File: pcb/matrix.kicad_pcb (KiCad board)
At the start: 2 copper layers, 57.4 x 47.1 mm, 69 parts, among them J1 Conn_01x02, J2 USB_C_Receptacle_USB2.0_14P, SW1 SW_Push, SW2 SW_Push, SW3 SW_Push, SW4 SW_Push, U1 ESP32-S3-MINI-1U, U2 AP2112K-3.3

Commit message: Update silkscreen
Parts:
- renumbered TP9 to 3V3, TP8 to BAT, TP1 to CP1, TP2 to CP2, TP3 to CP3, TP4 to CP4, TP5 to CP5, TP6 to CP6, TP7 to GND, TP10 to USB
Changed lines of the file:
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@@
 			(at 0 -1.43 90)
 			(layer "F.SilkS")
+			(hide yes)
 			(effects
 				(font
@@
 			(at 0 -1.43 0)
 			(layer "F.SilkS")
+			(hide yes)
 			(effects
 				(font
@@
 			(at 0 -1.43 0)
 			(layer "F.SilkS")
+			(hide yes)
 			(effects
 				(font
@@
 		(descr "SMD pad as test Point, diameter 1.0mm")
 		(tags "test point SMD pad")
-		(property "Reference" "TP7"
+		(property "Reference" "GND"
 			(at 0 -1.448 0)
 			(layer "F.SilkS")
@@
 			(at 0 -1.43 90)
 			(layer "F.SilkS")
+			(hide yes)
 			(effects
 				(font
@@
 			(at 0 -1.43 0)
 			(layer "F.SilkS")
+			(hide yes)
 			(effects
 				(font
@@
 			(at 0 -1.43 90)
 			(layer "F.SilkS")
+			(hide yes)
 			(effects
 				(font
@@
 			(at 0 -1.43 90)
 			(layer "F.SilkS")
+			(hide yes)
 			(effects
 				(font
@@
 			(at 0 -1.68 90)
 			(layer "F.SilkS")
+			(hide yes)
 			(effects
 				(font
@@
 			(at 0 -1.43 90)
 			(layer "F.SilkS")
+			(hide yes)
 			(effects
 				(font
@@
 			(at 0.0375 -1.68 90)
 			(layer "F.SilkS")
+			(hide yes)
 			(effects
 				(font
@@
 			(at 0 -1.68 90)
 			(layer "F.SilkS")
+			(hide yes)
 			(effects
 				(font
@@
 			(at 0 -1.68 90)
 			(layer "F.SilkS")
+			(hide yes)
 			(effects
 				(font
@@
 		(descr "SMD pad as test Point, diameter 1.0mm")
 		(tags "test point SMD pad")
-		(property "Reference" "TP4"
+		(property "Reference" "CP4"
 			(at 0 -1.448 0)
 			(layer "F.SilkS")
@@
 			(at 0 -1.43 0)
 			(layer "F.SilkS")
+			(hide yes)
 			(effects
 				(font
@@
 		(descr "SMD pad as test Point, diameter 1.0mm")
 		(tags "test point SMD pad")
-		(property "Reference" "TP6"
+		(property "Reference" "CP6"
 			(at 0 -1.448 0)
 			(layer "F.SilkS")
@@
 			(at 0 -1.43 90)
 			(layer "F.SilkS")
+			(hide yes)
 			(effects
 				(font
@@
 			(at 0 -1.43 90)
 			(layer "F.SilkS")
+			(hide yes)
 			(effects
 				(font
@@
 			(at 0 -1.68 90)
 			(layer "F.SilkS")
+			(hide yes)
 			(effects
 				(font
@@
 			(at 0 -1.43 0)
 			(layer "F.SilkS")
+			(hide yes)
 			(effects
 				(font
@@
 			(at 0 -1.43 90)
 			(layer "F.SilkS")
+			(hide yes)
 			(effects
 				(font
@@
 			(at 0 -1.43 90)
 			(layer "F.SilkS")
+			(hide yes)
 			(effects
 				(font
@@
 			(at 0 -1.43 0)
 			(layer "F.SilkS")
+			(hide yes)
 			(effects
 				(font
@@
 			(at 0 -1.43 0)
 			(layer "F.SilkS")
+			(hide yes)
 			(effects
 				(font
@@
 			(at 0 -1.43 90)
 			(layer "F.SilkS")
+			(hide yes)
 			(effects
 				(font
@@
 			(at 0 -1.68 90)
 			(layer "F.SilkS")
+			(hide yes)
 			(effects
 				(font
@@
 			(at 0 -1.43 0)
 			(layer "F.SilkS")
+			(hide yes)
 			(effects
 				(font
@@
 			(at 0 -1.68 90)
 			(layer "F.SilkS")
+			(hide yes)
 			(effects
 				(font
@@
 			(at 0 -1.43 0)
 			(layer "F.SilkS")
+			(hide yes)
 			(effects
 				(font
@@
 			(at 0 -1.43 0)
 			(layer "F.SilkS")
+			(hide yes)
 			(effects
 				(font
@@
 			(at 0 -1.68 90)
 			(layer "F.SilkS")
+			(hide yes)
 			(effects
 				(font
@@
 		(descr "SMD pad as test Point, diameter 1.0mm")
 		(tags "test point SMD pad")
-		(property "Reference" "TP9"
+		(property "Reference" "3V3"
 			(at 0 -1.448 0)
 			(layer "F.SilkS")
@@
 			(at 0 -1.43 0)
 			(layer "F.SilkS")
+			(hide yes)
 			(effects
 				(font
@@
 		(descr "SMD pad as test Point, diameter 1.0mm")
 		(tags "test point SMD pad")
-		(property "Reference" "TP2"
+		(property "Reference" "CP2"
 			(at 0 -1.448 0)
 			(layer "F.SilkS")
@@
 			(at 0 -1.68 90)
 			(layer "F.SilkS")
+			(hide yes)
 			(effects
 				(font
@@
 			(at 0 -1.43 90)
 			(layer "F.SilkS")
+			(hide yes)
 			(effects
 				(font
@@
 			(at 0 -1.43 90)
 			(layer "F.SilkS")
+			(hide yes)
 			(effects
 				(font
@@
 		(descr "SMD pad as test Point, diameter 1.0mm")
 		(tags "test point SMD pad")
-		(property "Reference" "TP10"
+		(property "Reference" "USB"
 			(at 0 -1.448 0)
 			(layer "F.SilkS")
@@
 			(at 0 -1.68 90)
 			(layer "F.SilkS")
+			(hide yes)
 			(effects
 				(font
@@
 			(at 0 -1.68 90)
 			(layer "F.SilkS")
+			(hide yes)
 			(effects
 				(font
@@
 			(at 0 -1.68 90)
 			(layer "F.SilkS")
+			(hide yes)
 			(effects
 				(font
@@
 			(at 0 -1.43 0)
 			(layer "F.SilkS")
+			(hide yes)
 			(effects
 				(font
@@
 			(at 0 -1.68 90)
 			(layer "F.SilkS")
+			(hide yes)
 			(effects
 				(font
@@
 			(at 0 -1.68 90)
 			(layer "F.SilkS")
+			(hide yes)
 			(effects
 				(font
@@
 		(descr "SMD pad as test Point, diameter 1.0mm")
 		(tags "test point SMD pad")
-		(property "Reference" "TP5"
+		(property "Reference" "CP5"
 			(at 0 -1.448 0)
 			(layer "F.SilkS")
@@
 			(at 0 -1.43 0)
 			(layer "F.SilkS")
+			(hide yes)
 			(effects
 				(font
@@
 			(at 0 -1.43 0)
 			(layer "F.SilkS")
+			(hide yes)
 			(effects
 				(font
@@
 		(descr "SMD pad as test Point, diameter 1.0mm")
 		(tags "test point SMD pad")
-		(property "Reference" "TP8"
+		(property "Reference" "BAT"
 			(at 0 -1.448 0)
 			(layer "F.SilkS")
@@
 		(descr "SMD pad as test Point, diameter 1.0mm")
 		(tags "test point SMD pad")
-		(property "Reference" "TP3"
+		(property "Reference" "CP3"
 			(at 0 -1.447869 0)
 			(layer "F.SilkS")
@@
 			(at 0 -1.68 90)
 			(layer "F.SilkS")
+			(hide yes)
 			(effects
 				(font
@@
 			(at 0.0375 -1.68 90)
 			(layer "F.SilkS")
+			(hide yes)
 			(effects
 				(font
@@
 			(at 0 -1.43 0)
 			(layer "F.SilkS")
+			(hide yes)
 			(effects
 				(font
@@
 			(at 0 -1.68 90)
 			(layer "F.SilkS")
+			(hide yes)
 			(effects
 				(font
@@
 			(at 0.0375 -1.68 90)
 			(layer "F.SilkS")
+			(hide yes)
 			(effects
 				(font
@@
 			(at 0.0375 -1.68 90)
 			(layer "F.SilkS")
+			(hide yes)
 			(effects
 				(font
@@
 		(descr "SMD pad as test Point, diameter 1.0mm")
 		(tags "test point SMD pad")
-		(property "Reference" "TP1"
+		(property "Reference" "CP1"
 			(at 0 -1.448 0)
 			(layer "F.SilkS")
@@
 			(at 0 -1.43 0)
 			(layer "F.SilkS")
+			(hide yes)
 			(effects
 				(font
@@
 			(at 0 -1.43 0)
 			(layer "F.SilkS")
+			(hide yes)
 			(effects
 				(font
@@
 			(at 0 -1.43 0)
 			(layer "F.SilkS")
+			(hide yes)
 			(effects
 				(font
@@
 			(at 0.0375 -1.68 90)
 			(layer "F.SilkS")
+			(hide yes)
 			(effects
 				(font
@@
 			(at 0 -1.43 0)
 			(layer "F.SilkS")
+			(hide yes)
 			(effects
 				(font

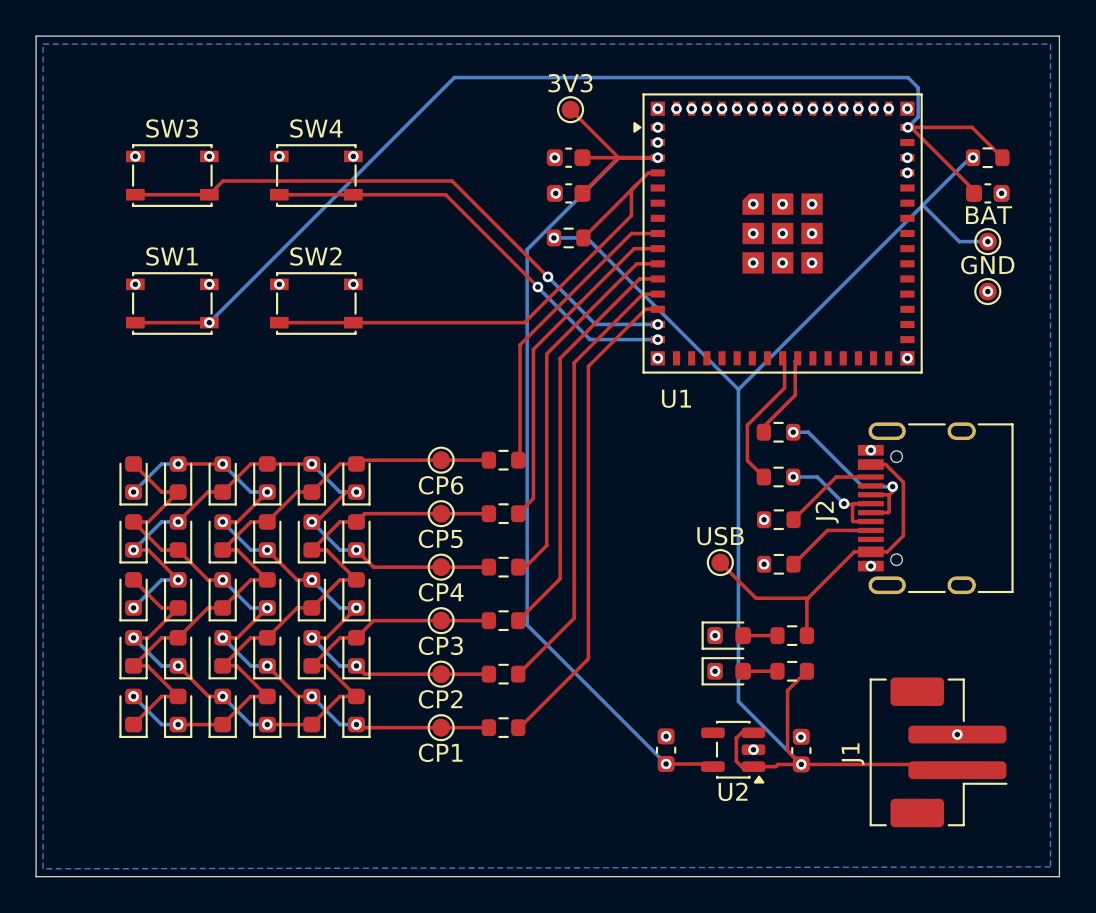
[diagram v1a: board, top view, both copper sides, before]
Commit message: Fix incorrect voltage
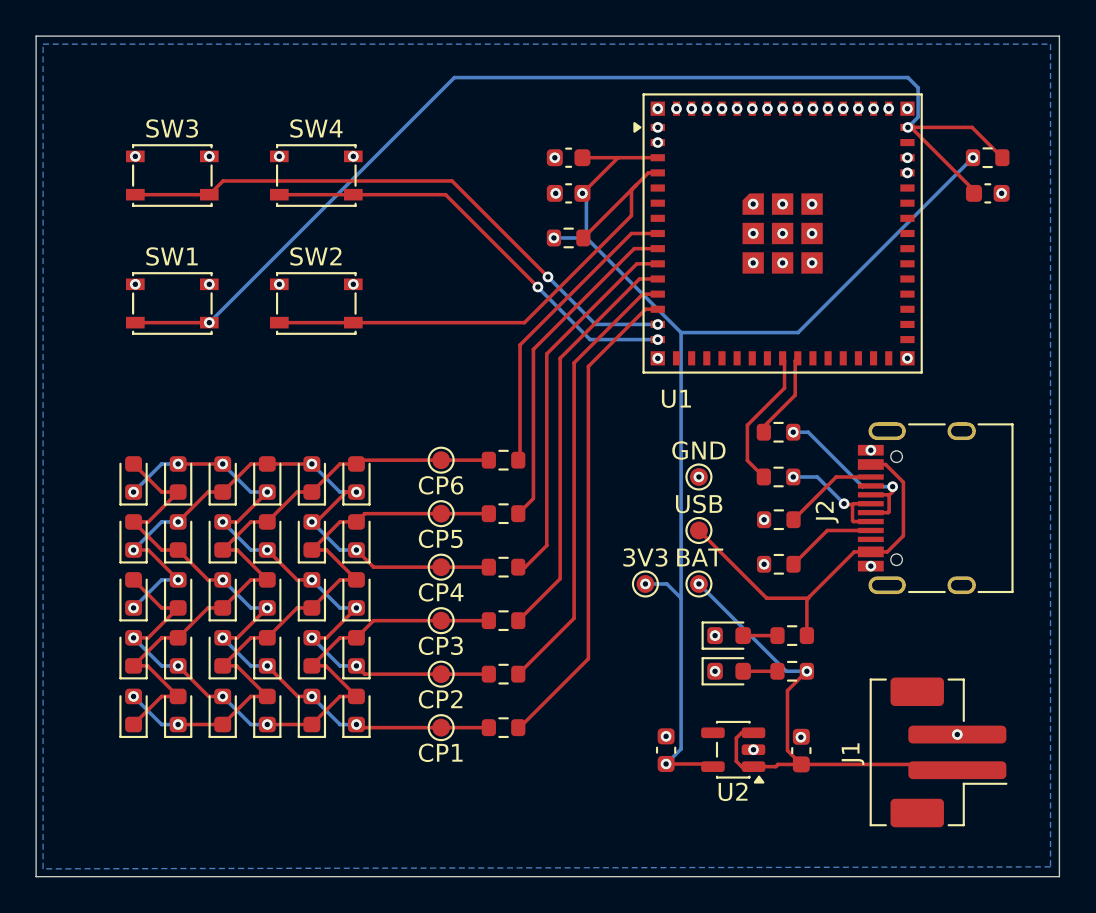
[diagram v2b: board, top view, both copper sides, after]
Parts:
- moved 3V3 26.9 mm to (149.2, 108.0)
- moved BAT 25.1 mm to (152.2, 108.0)
- moved GND 19.3 mm to (152.2, 102.0)
- moved USB 2.16 mm to (152.2, 105.0)
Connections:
- R3 pad 2: Net-(J1-Pin_1) -> Net-(U1-3V3)
- R4 pad 2: Net-(J1-Pin_1) -> Net-(U1-3V3)
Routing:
- net Net-(J1-Pin_1): track 80.9 -> 29.5 mm, vias 4 -> 2
- net Net-(U1-3V3): track 57.3 -> 69.1 mm, vias 2 -> 5
- net Net-(J2-VBUS-PadA4): track 20.0 -> 21.9 mm
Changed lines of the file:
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@@
 			(layers "F.Cu" "F.Mask" "F.Paste")
 			(roundrect_rratio 0.25)
-			(net 1 "Net-(J1-Pin_1)")
+			(net 3 "Net-(U1-3V3)")
 			(pintype "passive")
 		)
@@
 	(footprint "TestPoint:TestPoint_Pad_D1.0mm"
 		(layer "F.Cu")
-		(at 168.4 91.6)
+		(at 152.2 102)
 		(descr "SMD pad as test Point, diameter 1.0mm")
 		(tags "test point SMD pad")
@@
 			(layers "F.Cu" "F.Mask" "F.Paste")
 			(roundrect_rratio 0.25)
-			(net 1 "Net-(J1-Pin_1)")
+			(net 3 "Net-(U1-3V3)")
 			(pintype "passive")
 		)
@@
 	(footprint "TestPoint:TestPoint_Pad_D1.0mm"
 		(layer "F.Cu")
-		(at 145 81.4)
+		(at 149.2 108)
 		(descr "SMD pad as test Point, diameter 1.0mm")
 		(tags "test point SMD pad")
@@
 	(footprint "TestPoint:TestPoint_Pad_D1.0mm"
 		(layer "F.Cu")
-		(at 153.4 106.8)
+		(at 152.2 105)
 		(descr "SMD pad as test Point, diameter 1.0mm")
 		(tags "test point SMD pad")
@@
 	(footprint "TestPoint:TestPoint_Pad_D1.0mm"
 		(layer "F.Cu")
-		(at 168.4 88.8)
+		(at 152.2 108)
 		(descr "SMD pad as test Point, diameter 1.0mm")
 		(tags "test point SMD pad")
@@
 	)
 	(segment
-		(start 167.5675 84.095)
-		(end 167.4175 84.095)
-		(width 0.2)
-		(layer "F.Cu")
-		(net 1)
-	)
-	(segment
 		(start 156.51 118.245)
 		(end 156.635 118.12)
@@
 	)
 	(via
-		(at 167.5675 84.095)
-		(size 0.6)
-		(drill 0.3)
-		(layers "F.Cu" "B.Cu")
-		(net 1)
-	)
-	(via
-		(at 168.4 88.8)
-		(size 0.6)
-		(drill 0.3)
-		(layers "F.Cu" "B.Cu")
-		(net 1)
-	)
-	(via
-		(at 157.9425 118.12)
+		(at 158.254265 112.895735)
 		(size 0.6)
 		(drill 0.3)
@@
 	)
 	(via
-		(at 144.0675 88.595)
+		(at 152.2 108)
 		(size 0.6)
 		(drill 0.3)
@@
 	)
 	(segment
-		(start 167.5675 84.095)
-		(end 167.4175 84.095)
-		(width 0.2)
-		(layer "B.Cu")
-		(net 1)
-	)
-	(segment
-		(start 167.4175 84.095)
-		(end 165.05625 86.45625)
-		(width 0.2)
-		(layer "B.Cu")
-		(net 1)
-	)
-	(segment
-		(start 154.4175 97.095)
-		(end 145.9175 88.595)
-		(width 0.2)
-		(layer "B.Cu")
-		(net 1)
-	)
-	(segment
-		(start 168.4 88.8)
-		(end 166.8 88.8)
-		(width 0.2)
-		(layer "B.Cu")
-		(net 1)
-	)
-	(segment
-		(start 154.4175 114.595)
-		(end 154.4175 97.095)
-		(width 0.2)
-		(layer "B.Cu")
-		(net 1)
-	)
-	(segment
-		(start 145.9175 88.595)
-		(end 144.0675 88.595)
-		(width 0.2)
-		(layer "B.Cu")
-		(net 1)
-	)
-	(segment
-		(start 166.8 88.8)
-		(end 164.75625 86.75625)
-		(width 0.2)
-		(layer "B.Cu")
-		(net 1)
-	)
-	(segment
-		(start 165.05625 86.45625)
-		(end 164.75625 86.75625)
-		(width 0.2)
-		(layer "B.Cu")
-		(net 1)
-	)
-	(segment
-		(start 157.9425 118.12)
-		(end 154.4175 114.595)
+		(start 158.254265 112.895735)
+		(end 157.095735 112.895735)
 		(width 0.2)
 		(layer "B.Cu")
@@
 	)
 	(segment
-		(start 164.75625 86.75625)
-		(end 154.4175 97.095)
+		(start 157.095735 112.895735)
+		(end 152.2 108)
 		(width 0.2)
 		(layer "B.Cu")
@@
 	)
 	(via
-		(at 168.4 91.6)
+		(at 152.2 102)
 		(size 0.6)
 		(drill 0.3)
@@
 	)
 	(segment
+		(start 145.6675 84.095)
+		(end 149.8925 84.095)
+		(width 0.2)
+		(layer "F.Cu")
+		(net 3)
+	)
+	(segment
 		(start 152.835735 118.095735)
 		(end 152.985 118.245)
@@
 	)
 	(segment
-		(start 145.6675 84.095)
-		(end 149.8925 84.095)
-		(width 0.2)
-		(layer "F.Cu")
-		(net 3)
-	)
-	(segment
-		(start 145 81.4)
-		(end 147.695 84.095)
+		(start 167.5675 84.095)
+		(end 167.4175 84.095)
 		(width 0.2)
 		(layer "F.Cu")
@@
 		(net 3)
 	)
-	(segment
-		(start 147.695 84.095)
-		(end 149.8925 84.095)
-		(width 0.2)
-		(layer "F.Cu")
+	(via
+		(at 167.5675 84.095)
+		(size 0.6)
+		(drill 0.3)
+		(layers "F.Cu" "B.Cu")
+		(net 3)
+	)
+	(via
+		(at 149.2 108)
+		(size 0.6)
+		(drill 0.3)
+		(layers "F.Cu" "B.Cu")
 		(net 3)
 	)
 	(via
-		(at 149.8925 84.095)
+		(at 144.0675 88.595)
 		(size 0.6)
 		(drill 0.3)
@@
 		(net 3)
 	)
+	(via
+		(at 145.6675 86.095)
+		(size 0.6)
+		(drill 0.3)
+		(layers "F.Cu" "B.Cu")
+		(net 3)
+	)
+	(segment
+		(start 157.759943 93.902557)
+		(end 167.5675 84.095)
+		(width 0.2)
+		(layer "B.Cu")
+		(net 3)
+	)
 	(segment
-		(start 142.5665 89.246057)
-		(end 147.717557 84.095)
+		(start 151.2 93.902557)
+		(end 145.892443 88.595)
 		(width 0.2)
 		(layer "B.Cu")
@@
 	(segment
 		(start 150.359265 118.095735)
-		(end 142.5665 110.30297)
+		(end 151.2 117.255)
 		(width 0.2)
 		(layer "B.Cu")
@@
 	)
 	(segment
-		(start 147.717557 84.095)
-		(end 149.8925 84.095)
+		(start 149.2 108)
+		(end 150.4 108)
+		(width 0.2)
+		(layer "B.Cu")
+		(net 3)
+	)
+	(segment
+		(start 145.892443 88.595)
+		(end 145.892443 86.319943)
+		(width 0.2)
+		(layer "B.Cu")
+		(net 3)
+	)
+	(segment
+		(start 151.2 108.8)
+		(end 151.2 93.902557)
+		(width 0.2)
+		(layer "B.Cu")
+		(net 3)
+	)
+	(segment
+		(start 145.892443 86.319943)
+		(end 145.6675 86.095)
+		(width 0.2)
+		(layer "B.Cu")
+		(net 3)
+	)
+	(segment
+		(start 145.892443 88.595)
+		(end 144.0675 88.595)
+		(width 0.2)
+		(layer "B.Cu")
+		(net 3)
+	)
+	(segment
+		(start 151.2 93.902557)
+		(end 157.759943 93.902557)
 		(width 0.2)
 		(layer "B.Cu")
@@
 	)
 	(segment
-		(start 142.5665 110.30297)
-		(end 142.5665 89.246057)
+		(start 151.2 117.255)
+		(end 151.2 108.8)
+		(width 0.2)
+		(layer "B.Cu")
+		(net 3)
+	)
+	(segment
+		(start 150.4 108)
+		(end 151.2 108.8)
 		(width 0.2)
 		(layer "B.Cu")
@@
 	)
 	(segment
-		(start 162.765 106.2)
-		(end 163.666002 105.298998)
+		(start 158.315 108.8)
+		(end 156 108.8)
 		(width 0.2)
 		(layer "F.Cu")
@@
 	)
 	(segment
-		(start 155.4 108.8)
-		(end 153.4 106.8)
+		(start 162.765 106.2)
+		(end 163.666002 105.298998)
 		(width 0.2)
 		(layer "F.Cu")
@@
 	)
 	(segment
-		(start 158.315 108.8)
-		(end 155.4 108.8)
+		(start 156 108.8)
+		(end 152.2 105)
 		(width 0.2)
 		(layer "F.Cu")
